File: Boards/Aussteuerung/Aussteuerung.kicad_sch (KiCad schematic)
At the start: 17 parts

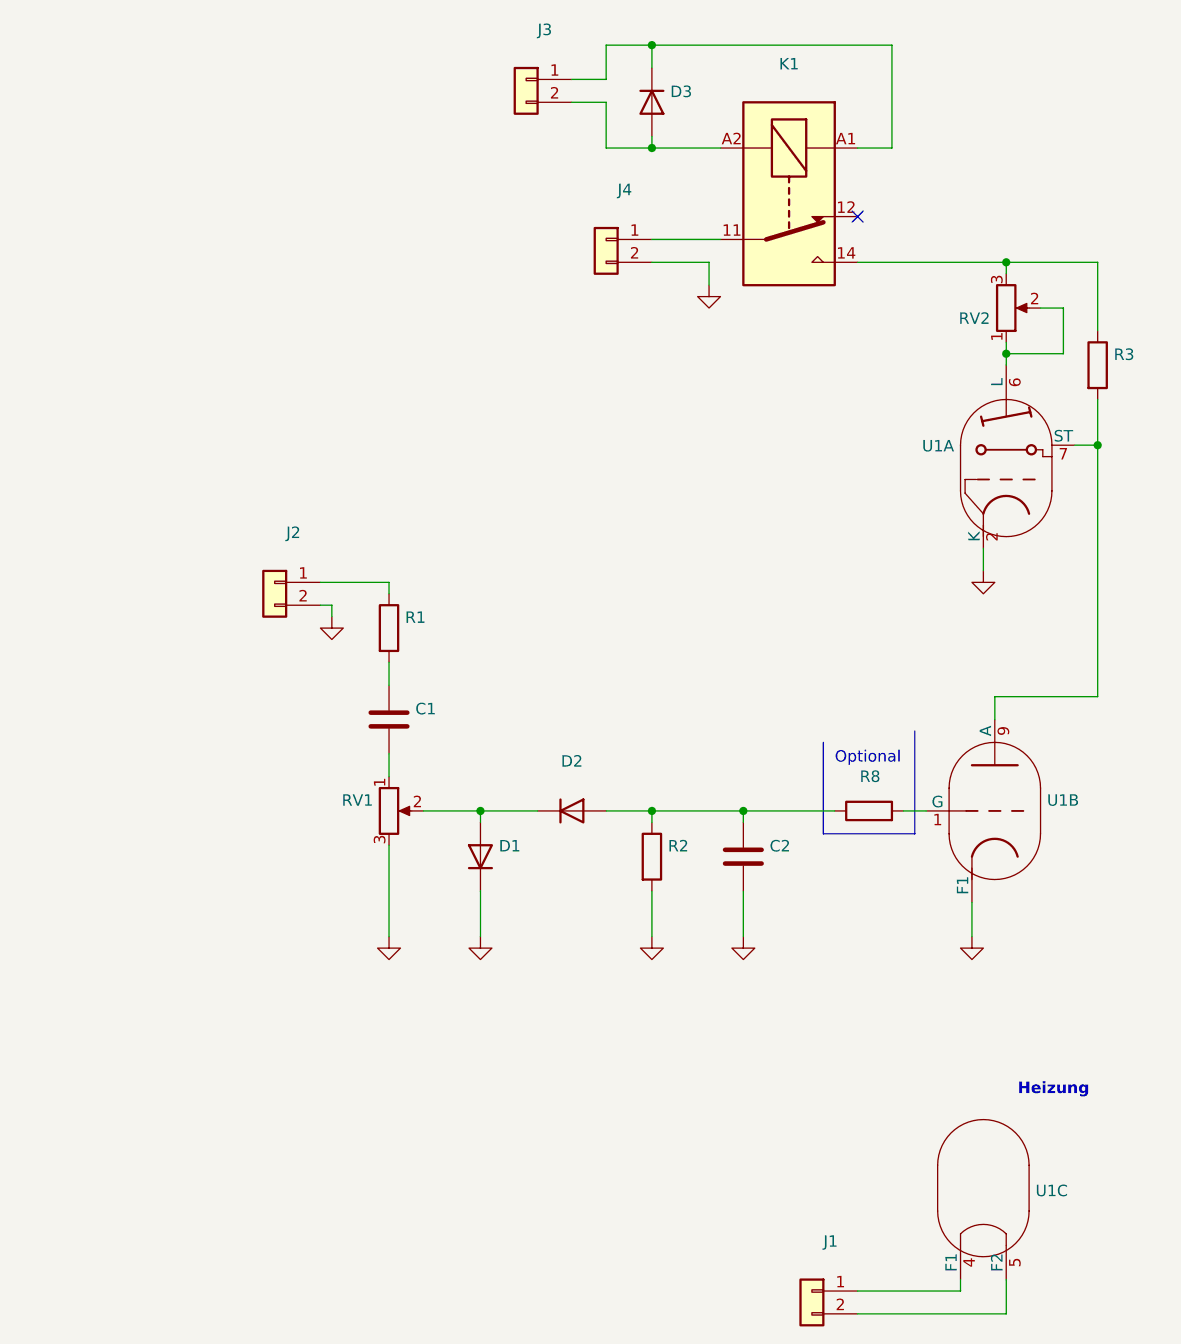
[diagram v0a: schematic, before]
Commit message: 6.3V, 400V und 400V Regler Boards bestellt
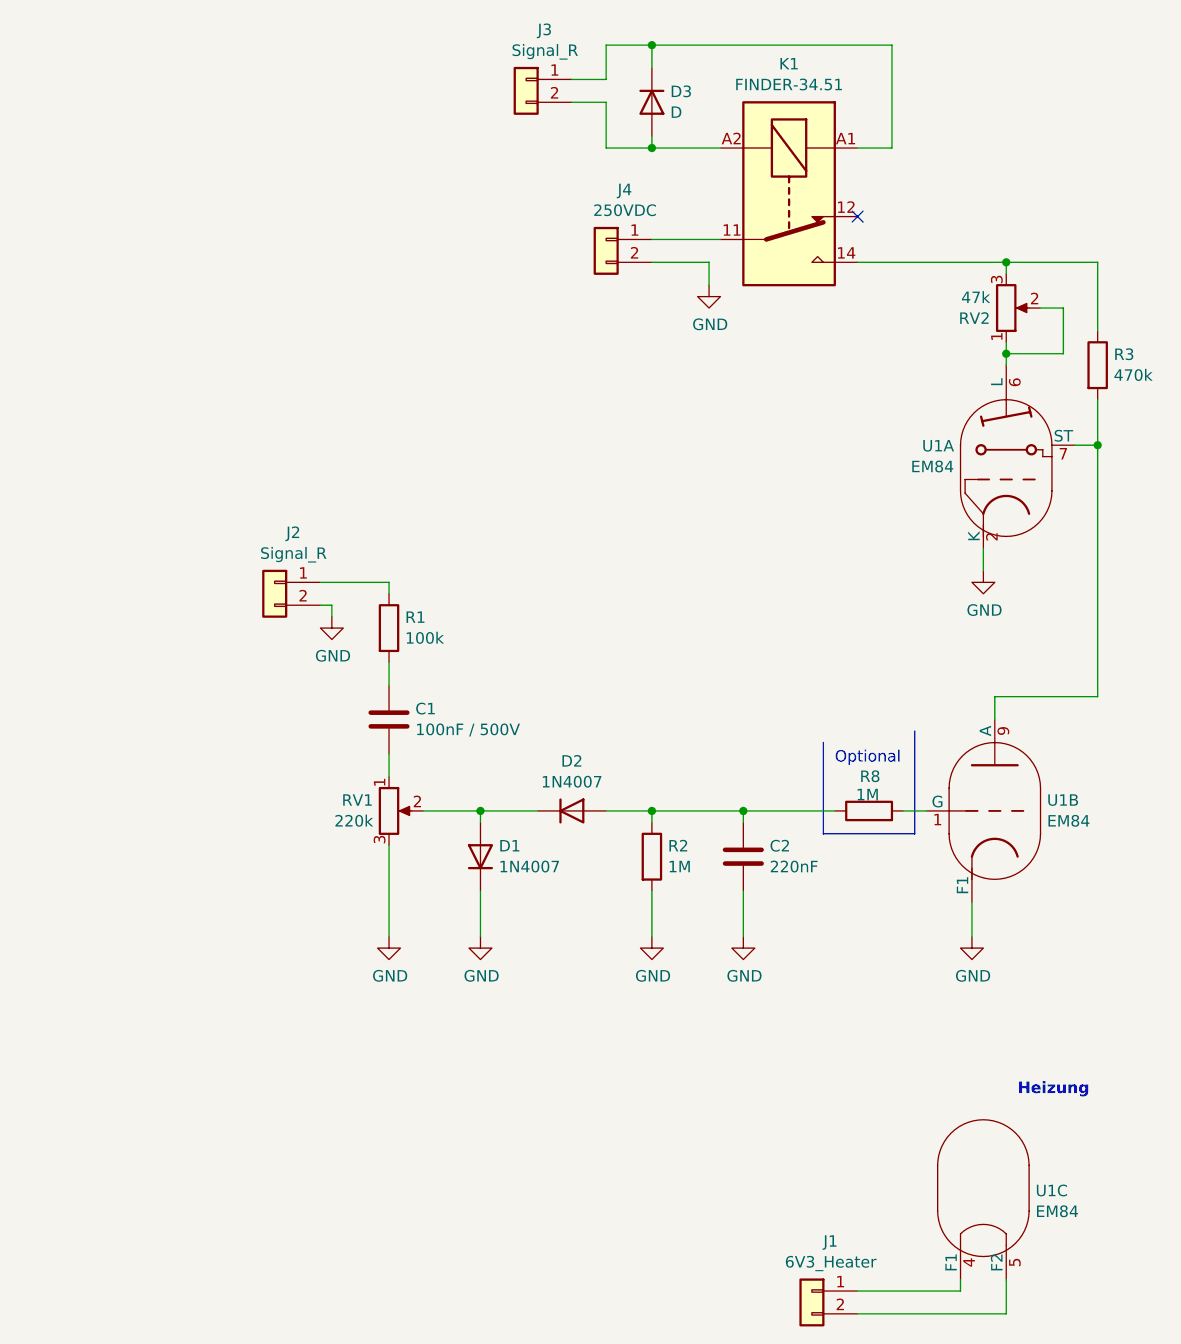
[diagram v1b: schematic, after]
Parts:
- C1: value (none) -> 100nF / 500V; footprint (none) -> Capacitor_THT:C_Disc_D5.0mm_W2.5mm_P5.00mm
- C2: value (none) -> 220nF; footprint (none) -> Capacitor_THT:C_Disc_D5.0mm_W2.5mm_P5.00mm
- D1, D2: value (none) -> 1N4007; footprint (none) -> Diode_THT:D_DO-35_SOD27_P10.16mm_Horizontal
- D3: value (none) -> D; footprint (none) -> Diode_THT:D_DO-35_SOD27_P10.16mm_Horizontal
- J1: value (none) -> 6V3_Heater; footprint (none) -> Connector_Molex:Molex_Mini-Fit_Jr_5566-02A_2x01_P4.20mm_Vertical
- J2: value (none) -> Signal_R; footprint (none) -> Connector_Molex:Molex_Mini-Fit_Jr_5566-02A_2x01_P4.20mm_Vertical
- J3: value (none) -> Signal_R; footprint (none) -> Connector_Molex:Molex_KK-254_AE-6410-02A_1x02_P2.54mm_Vertical
- J4: value (none) -> 250VDC; footprint (none) -> Connector_Molex:Molex_Mini-Fit_Jr_5566-02A_2x01_P4.20mm_Vertical
- K1: value (none) -> FINDER-34.51; footprint (none) -> Relay_THT:Relay_SPDT_Finder_34.51_Vertical
- R1: value (none) -> 100k; footprint (none) -> Resistor_THT:R_Axial_DIN0207_L6.3mm_D2.5mm_P10.16mm_Horizontal
- R2, R8: value (none) -> 1M; footprint (none) -> Resistor_THT:R_Axial_DIN0207_L6.3mm_D2.5mm_P10.16mm_Horizontal
- R3: value (none) -> 470k; footprint (none) -> Resistor_THT:R_Axial_DIN0207_L6.3mm_D2.5mm_P10.16mm_Horizontal
- RV1: value (none) -> 220k; footprint (none) -> Potentiometer_THT:Potentiometer_Piher_PT-10-V10_Vertical_Hole
- RV2: value (none) -> 47k; footprint (none) -> Potentiometer_THT:Potentiometer_Piher_PT-10-V10_Vertical_Hole
- U1: value (none) -> EM84; footprint (none) -> Valve:Valve_Noval_P
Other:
- company: (none) -> fordprfkt@googlemail.com
- title: (none) -> KT88 Amp / Aussteuerung

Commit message: Leiterplatten erstellt
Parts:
- added K2: FINDER-34.51, Relay_THT:Relay_SPDT_Finder_34.51_Vertical, symbol Relay:FINDER-34.51
- C1: footprint Capacitor_THT:C_Disc_D5.0mm_W2.5mm_P5.00mm -> Capacitor_THT:C_Rect_L26.5mm_W7.0mm_P22.50mm_MKS4
- C2: value 220nF -> 220nF/500V; footprint Capacitor_THT:C_Disc_D5.0mm_W2.5mm_P5.00mm -> Capacitor_THT:C_Rect_L26.5mm_W8.5mm_P22.50mm_MKS4
- J3: value Signal_R -> Enable
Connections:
- net GND: now also U1.3 (K); no longer U1.2 (K), U1.~ (F1)
- net at J2.1 (Pin_1): now also K2.11; no longer R1.1
- net at D3.1 (K), J3.1 (Pin_1), K1.A1: now also K2.A1
- net at D3.2 (A), J3.2 (Pin_2), K1.A2: now also K2.A2
- new net: K2.14, R1.1
- no-connect marks 1 -> 3
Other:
- moved on the sheet: D3, J2, J3, R8
